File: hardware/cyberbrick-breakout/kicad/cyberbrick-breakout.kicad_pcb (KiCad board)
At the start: 2 copper layers, 85 x 70 mm, 33 parts, among them J1 LX, J10 DL_LEFT, J11 DL_RIGHT, J12 DL_DOWN, J13 DR_UP, J14 DR_LEFT, J15 DR_RIGHT, J16 DR_DOWN, J17 SHL1, J18 SHL2, J19 SHR1, J2 LY, J20 SHR2, J21 START, J22 SELECT, J23 HOTKEY, J24 COIN, J3 RX, J4 RY, J6 MCP_BTNS, J7 I2C, J8 PWR_IN, J9 DL_UP, U1A ESP32-C3 top, U1B ESP32-C3 bot

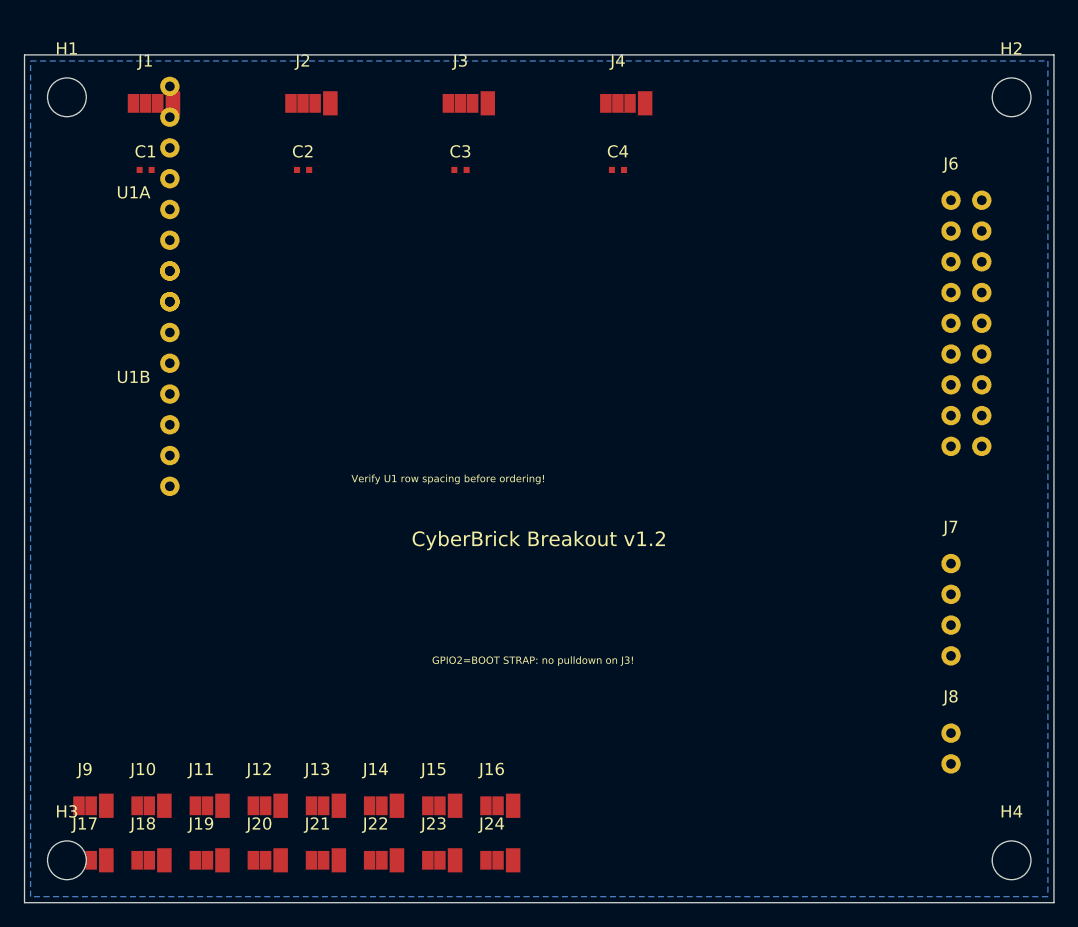
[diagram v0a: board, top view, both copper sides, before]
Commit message: Redesign PCB: 60x36mm, ESP32-C3 on B.Cu, USB-C right, display faces front
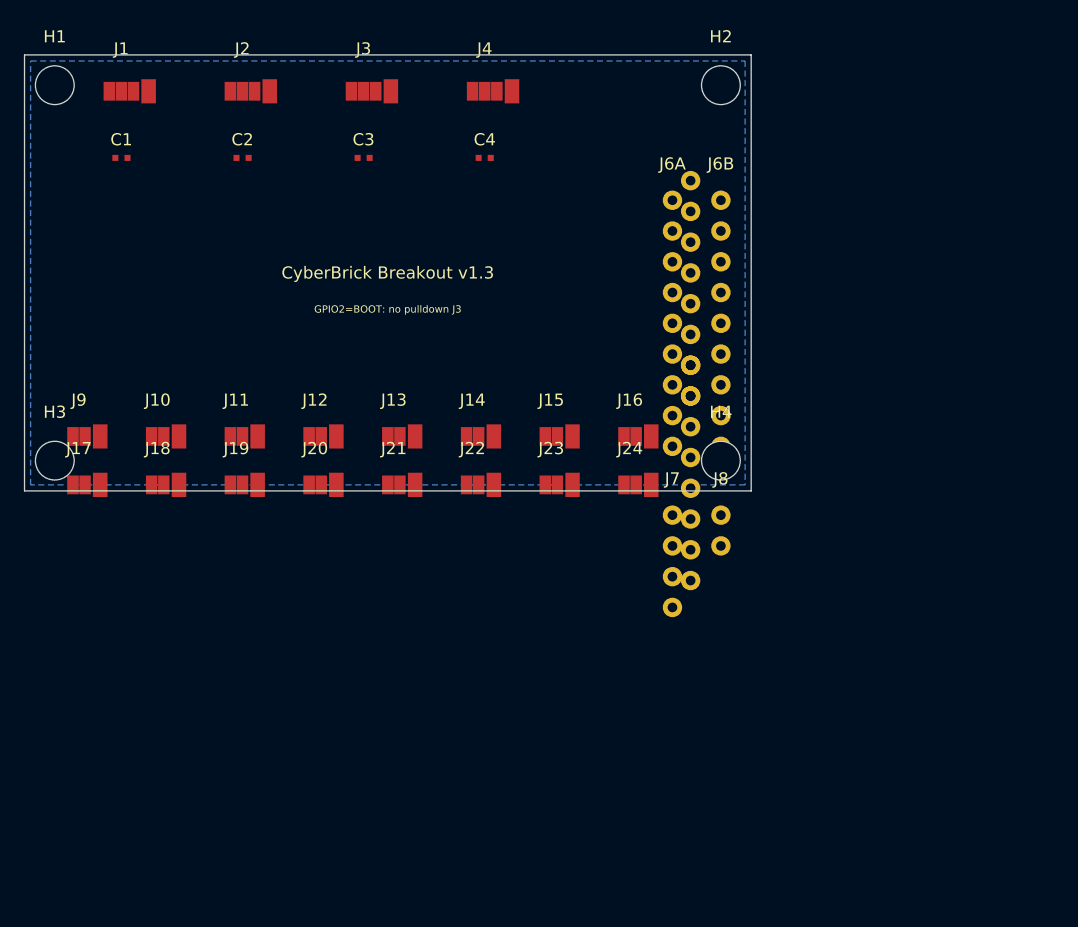
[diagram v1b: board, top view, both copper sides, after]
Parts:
- removed J6: MCP_BTNS, Connector_PinHeader_2.54mm:PinHeader_2x09_P2.54mm_Vertical
- added J6A: GPA, Connector_PinHeader_2.54mm:PinHeader_1x09_P2.54mm_Vertical, F.Cu at (53.5, 12.0)
- added J6B: GPB, Connector_PinHeader_2.54mm:PinHeader_1x09_P2.54mm_Vertical, F.Cu at (57.5, 12.0)
- J10: value DL_LEFT -> DL_LFT
- J11: value DL_RIGHT -> DL_RGT
- J12: value DL_DOWN -> DL_DWN
- J14: value DR_LEFT -> DR_LFT
- J15: value DR_RIGHT -> DR_RGT
- J16: value DR_DOWN -> DR_DWN
- J22: value SELECT -> SEL
- J8: value PWR_IN -> PWR
- U1A, U1B: moved to B.Cu
- moved U1A 44.1 mm to (55.0, 10.4), turned to 270 degrees
- moved U1B 44.1 mm to (55.0, 25.6), turned to 270 degrees
- moved H4 40.8 mm to (57.5, 33.5)
- moved J24 33.0 mm to (50.0, 35.5)
- moved H3 33.0 mm to (2.50, 33.5)
- moved J16 32.6 mm to (50.0, 31.5)
- moved J23 32.5 mm to (43.5, 35.5)
- moved J22 32.0 mm to (37.0, 35.5)
- moved J15 32.0 mm to (43.5, 31.5)
- moved J21 31.6 mm to (30.5, 35.5)
- moved J14 31.5 mm to (37.0, 31.5)
- moved J20 31.3 mm to (24.0, 35.5)
- moved J13 31.1 mm to (30.5, 31.5)
- moved J19 31.1 mm to (17.5, 35.5)
- moved J18 31.0 mm to (11.0, 35.5)
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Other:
- board size 85 x 70 mm -> 60 x 36 mm
- board text added: "CyberBrick Breakout v1.3"
- board text added: "GPIO2=BOOT: no pulldown J3"
- board text added: "Verify U1 row spacing!"
- board text removed: "CyberBrick Breakout v1.2"
- board text removed: "GPIO2=BOOT STRAP: no pulldown on J3!"
- board text removed: "Verify U1 row spacing before ordering!"

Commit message: latest layout
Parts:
- moved J1 215.0 mm to (178.5, 134.0), turned to -90 degrees
- moved C1 207.7 mm to (173.5, 134.0), turned to -90 degrees
- moved J2 202.9 mm to (178.5, 127.0), turned to -90 degrees
- moved C2 195.5 mm to (173.5, 127.0), turned to -90 degrees
- moved J9 194.0 mm to (166.0, 139.0), turned to 180 degrees
- moved J3 190.7 mm to (178.5, 120.0), turned to -90 degrees
- moved J10 183.7 mm to (160.0, 139.0), turned to 180 degrees
- moved C3 183.6 mm to (173.5, 120.5), turned to -90 degrees
- moved J4 177.9 mm to (178.5, 112.0), turned to -90 degrees
- moved J17 177.5 mm to (167.0, 107.0), turned to 180 degrees
- moved J11 173.4 mm to (153.5, 139.0), turned to 180 degrees
- moved C4 170.5 mm to (173.5, 112.0), turned to -90 degrees
- moved J18 165.7 mm to (160.5, 107.0), turned to 180 degrees
- moved J6A 163.7 mm to (160.3, 136.0), turned to -90 degrees
- moved J12 163.4 mm to (147.0, 139.0), turned to 180 degrees
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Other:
- board size 60 x 36 mm -> 73 x 41 mm
